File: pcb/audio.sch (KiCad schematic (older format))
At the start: 0 parts

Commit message: pcb: working on sch
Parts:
- added C? (x4): 22uF, symbol Device:C
- added C? (x4): 620pF, symbol Device:C
- added C? (x4): 680pF, symbol Device:C
- added C? (x5): 10uF, symbol Device:C
- added C? (x2): 47uF, symbol Device:CP
- added J?: AudioJack3_Ground_SwitchTR, symbol Connector:AudioJack3_Ground_SwitchTR
- added R? (x4): 750, symbol Device:R
- added R? (x8): 4.99K, symbol Device:R
- added R? (x4): 2.67K, symbol Device:R
- added R? (x4): 2.43K, symbol Device:R
- added R? (x4): 6.81K, symbol Device:R
- added R? (x4): 100, symbol Device:R
- added R? (x4): 100K, symbol Device:R
- added R? (x4): 10K, symbol Device:R
- added R? (x2): 0, symbol Device:R
- added R?: 806, symbol Device:R
- added R?: 1K, symbol Device:R
- added RV?: R_POT_Dual, symbol Device:R_POT_Dual
- added U?: WM8740, footprints:SSOP-28-P0.65, symbol symbols:WM8740
- added U? (x9): ADA4075-2, symbol Amplifier_Operational:ADA4075-2
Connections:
- net labels added: DAC_SYSCLK, GND, SAI1_TXC, SAI1_TXD, SAI1_TXFS, VCOM
- wire segments 0 -> 161

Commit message: pcb: working on sch
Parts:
- removed C? (x4): 22uF, symbol Device:C
- removed C? (x4): 620pF, symbol Device:C
- removed C? (x4): 680pF, symbol Device:C
- removed C? (x5): 10uF, symbol Device:C
- removed C? (x2): 47uF, symbol Device:CP
- removed J?: AudioJack3_Ground_SwitchTR, symbol Connector:AudioJack3_Ground_SwitchTR
- removed R? (x4): 750, symbol Device:R
- removed R? (x8): 4.99K, symbol Device:R
- removed R? (x4): 2.67K, symbol Device:R
- removed R? (x4): 2.43K, symbol Device:R
- removed R? (x4): 6.81K, symbol Device:R
- removed R? (x4): 100, symbol Device:R
- removed R? (x4): 100K, symbol Device:R
- removed R? (x4): 10K, symbol Device:R
- removed R? (x2): 0, symbol Device:R
- removed R?: 806, symbol Device:R
- removed R?: 1K, symbol Device:R
- removed RV?: R_POT_Dual, symbol Device:R_POT_Dual
- removed U?: WM8740, footprints:SSOP-28-P0.65, symbol symbols:WM8740
- removed U? (x9): ADA4075-2, symbol Amplifier_Operational:ADA4075-2
- added C400, C401, C402, C403: 100nF, symbol Device:C
- added C404: 4.7uF, symbol Device:C
- added C405, C408, C409: 1uF, symbol Device:C
- added C406, C407, C412, C413, C414, C415, C416, C417: 2.2uF, symbol Device:C
- added C410, C411: 15uF, symbol Device:C
- added J400: AudioJack4, symbol Connector:AudioJack4
- added L400, L401: 120R, symbol Device:L
- added R400, R401, R402, R403: 33, symbol Device:R
- added R404: 10K, symbol Device:R
- added U400: CS43130, symbol symbols:CS43130
- added U401: ADP150-3.0, Package_TO_SOT_SMD:SOT-23-5, symbol Regulator_Linear:AP2127K-3.0
- added U402, U403: ADP150-1.8, Package_TO_SOT_SMD:SOT-23-5, symbol Regulator_Linear:AP2112K-1.8
- added X400: DSC1001CE2-022.5792, Oscillator:Oscillator_SMD_Abracon_ASE-4Pin_3.2x2.5mm, symbol Oscillator:ASE-xxxMHz
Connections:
- net labels added: +1V8, +3V3, I2C1_SCL, I2C1_SDA, POR, SAI1_MCLK
- net labels removed: DAC_SYSCLK, VCOM
- wire segments 161 -> 90
- no-connect marks 0 -> 4

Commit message: pcb: finishing sch for r0.1
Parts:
- added RV400: RK14J11A0A02, footprints:Potentiometer_RK14J, symbol Device:R_POT
- C400, C401, C402, C403, C405, C406, C407, C408, C409, C412, C413, C414, C415, C416, C417: footprint (none) -> Capacitor_SMD:C_0402_1005Metric
- C404, C410, C411: footprint (none) -> Capacitor_SMD:C_0603_1608Metric
- J400: footprint (none) -> Connector_Audio:Jack_3.5mm_PJ320D_Horizontal
- L400, L401: footprint (none) -> Inductor_SMD:L_0603_1608Metric
- R400, R401, R402, R403, R404: footprint (none) -> Resistor_SMD:R_0603_1608Metric
- U400: footprint (none) -> Package_DFN_QFN:QFN-40-1EP_5x5mm_P0.4mm_EP3.6x3.6mm_ThermalVias
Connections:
- net +3V3: now also RV400.1
- net GND: now also RV400.3
- new net ADC1_IN0: RV400.2

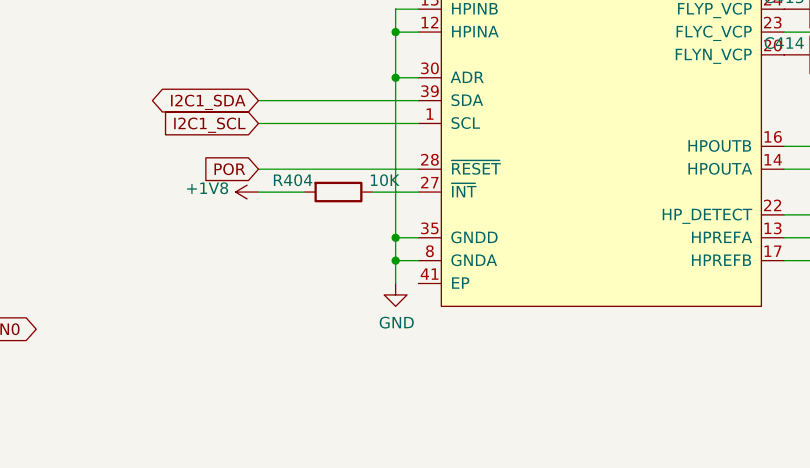
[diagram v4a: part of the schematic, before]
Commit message: pcb: initial netlist
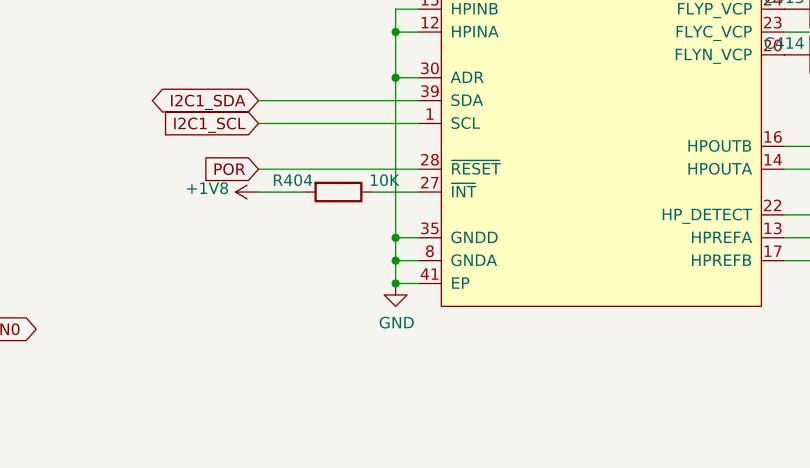
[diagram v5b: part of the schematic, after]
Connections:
- net GND: now also U400.41 (EP)
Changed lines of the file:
@@
 Wire Wire Line
 	2550 5900 2900 5900
+Wire Wire Line
+	5000 5700 4900 5700
+Connection ~ 4900 5700
 $EndSCHEMATC

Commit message: pcb: routing
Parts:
- removed J400: AudioJack4, Connector_Audio:Jack_3.5mm_PJ320D_Horizontal, symbol Connector:AudioJack4
- added J1: AudioJack3_SwitchTR, footprints:Jack_3.5mm_PJ307C, symbol pcb-rescue:AudioJack3_SwitchTR-Connector
- C400, C401, C402, C403, C404, C405, C406, C407, C408, C409, C410, C411, C412, C413, C414, C415, C416, C417: symbol Device:C -> pcb-rescue:C-Device
- L400, L401: symbol Device:L -> pcb-rescue:L-Device
- R400, R401, R402, R403, R404: symbol Device:R -> pcb-rescue:R-Device
- RV400: symbol Device:R_POT -> pcb-rescue:R_POT-Device
- U401: symbol Regulator_Linear:AP2127K-3.0 -> pcb-rescue:AP2127K-3.0-Regulator_Linear
- U402, U403: symbol Regulator_Linear:AP2112K-1.8 -> pcb-rescue:AP2112K-1.8-Regulator_Linear
- X400: symbol Oscillator:ASE-xxxMHz -> pcb-rescue:ASE-xxxMHz-Oscillator
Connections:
- net GND: now also U400.13 (HPREFA), U400.17 (HPREFB), J1.S
- net at U400.16 (HPOUTB): now also J1.R
- net at U400.22 (HP_DETECT): now also J1.TN
- net at U400.14 (HPOUTA): now also J1.T
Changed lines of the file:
@@
 SAI1_TXD
-$Comp
-L Connector:AudioJack4 J400
-U 1 1 5D3B8C10
-P 7850 5100
-F 0 "J400" H 7520 5075 50  0000 R CNN
-F 1 "AudioJack4" H 7520 4984 50  0000 R CNN
-F 2 "Connector_Audio:Jack_3.5mm_PJ320D_Horizontal" H 7850 5100 50  0001 C CNN
-F 3 "~" H 7850 5100 50  0001 C CNN
-	1    7850 5100
-	-1   0    0    -1
-$EndComp
 $Comp
 L symbols:CS43130 U400
@@
 $EndComp
 $Comp
-L Regulator_Linear:AP2112K-1.8 U402
+L pcb-rescue:AP2112K-1.8-Regulator_Linear U402
 U 1 1 5D3BE239
 P 8200 3500
@@
 $EndComp
 $Comp
-L Regulator_Linear:AP2127K-3.0 U401
+L pcb-rescue:AP2127K-3.0-Regulator_Linear U401
 U 1 1 5D3C4251
 P 8200 2500
@@
 $EndComp
 $Comp
-L power:+3V3 #PWR0252
+L pcb-rescue:+3V3-power #PWR0252
 U 1 1 5D3C5E19
 P 8600 2300
@@
 	8500 2500 8600 2500
 $Comp
-L power:GND #PWR0253
+L pcb-rescue:GND-power #PWR0253
 U 1 1 5D3C6CEC
 P 8200 2800
@@
 $EndComp
 $Comp
-L power:GND #PWR0254
+L pcb-rescue:GND-power #PWR0254
 U 1 1 5D3C71EE
 P 8200 3800
@@
 $EndComp
 $Comp
-L Device:C C405
+L pcb-rescue:C-Device C405
 U 1 1 5D3C76A9
 P 8900 2550
@@
 $EndComp
 $Comp
-L Device:C C408
+L pcb-rescue:C-Device C408
 U 1 1 5D3C8004
 P 8900 3550
@@
 $EndComp
 $Comp
-L Device:C C404
+L pcb-rescue:C-Device C404
 U 1 1 5D3C85BE
 P 7600 2550
@@
 $EndComp
 $Comp
-L Device:C C407
+L pcb-rescue:C-Device C407
 U 1 1 5D3C8D9A
 P 7700 3550
@@
 $EndComp
 $Comp
-L Device:C C406
+L pcb-rescue:C-Device C406
 U 1 1 5D3C9210
 P 7300 3650
@@
 $EndComp
 $Comp
-L Device:C C403
+L pcb-rescue:C-Device C403
 U 1 1 5D3C9FD4
 P 7200 2550
@@
 $EndComp
 $Comp
-L power:GND #PWR0255
+L pcb-rescue:GND-power #PWR0255
 U 1 1 5D3CA6E5
 P 7600 2700
@@
 $EndComp
 $Comp
-L power:GND #PWR0256
+L pcb-rescue:GND-power #PWR0256
 U 1 1 5D3CA8EB
 P 7200 2700
@@
 $EndComp
 $Comp
-L power:GND #PWR0257
+L pcb-rescue:GND-power #PWR0257
 U 1 1 5D3CAA8D
 P 8900 2700
@@
 $EndComp
 $Comp
-L power:GND #PWR0258
+L pcb-rescue:GND-power #PWR0258
 U 1 1 5D3CAE2F
 P 8900 3700
@@
 $EndComp
 $Comp
-L power:GND #PWR0259
+L pcb-rescue:GND-power #PWR0259
 U 1 1 5D3CB31E
 P 7700 3700
@@
 $EndComp
 $Comp
-L power:GND #PWR0260
+L pcb-rescue:GND-power #PWR0260
 U 1 1 5D3CB6C2
 P 7300 3800
@@
 Connection ~ 8600 2500
 $Comp
-L Device:C C410
+L pcb-rescue:C-Device C410
 U 1 1 5D3CDB2E
 P 6950 3300
@@
 $EndComp
 $Comp
-L Device:C C411
+L pcb-rescue:C-Device C411
 U 1 1 5D3CEBF2
 P 6950 3600
@@
 $EndComp
 $Comp
-L Device:C C412
+L pcb-rescue:C-Device C412
 U 1 1 5D3D16A3
 P 6950 3800
@@
 	6800 3800 6600 3800
 $Comp
-L Regulator_Linear:AP2112K-1.8 U403
+L pcb-rescue:AP2112K-1.8-Regulator_Linear U403
 U 1 1 5D3DDAF9
 P 8200 4400
@@
 Connection ~ 8600 4300
 $Comp
-L power:GND #PWR0261
+L pcb-rescue:GND-power #PWR0261
 U 1 1 5D3DDB03
 P 8200 4700
@@
 $EndComp
 $Comp
-L Device:C C409
+L pcb-rescue:C-Device C409
 U 1 1 5D3DDB09
 P 8900 4450
@@
 $EndComp
 $Comp
-L Device:C C417
+L pcb-rescue:C-Device C417
 U 1 1 5D3DDB0F
 P 7700 4450
@@
 $EndComp
 $Comp
-L power:GND #PWR0262
+L pcb-rescue:GND-power #PWR0262
 U 1 1 5D3DDB15
 P 8900 4600
@@
 $EndComp
 $Comp
-L power:GND #PWR0263
+L pcb-rescue:GND-power #PWR0263
 U 1 1 5D3DDB1B
 P 7700 4600
@@
 Connection ~ 7700 4300
 $Comp
-L Device:C C416
+L pcb-rescue:C-Device C416
 U 1 1 5D3E2D8A
 P 7400 4350
@@
 $EndComp
 $Comp
-L Device:C C415
+L pcb-rescue:C-Device C415
 U 1 1 5D3E3537
 P 7100 4450
@@
 $EndComp
 $Comp
-L Device:C C413
+L pcb-rescue:C-Device C413
 U 1 1 5D3E42FA
 P 6750 4500
@@
 $EndComp
 $Comp
-L Device:C C414
+L pcb-rescue:C-Device C414
 U 1 1 5D3E4B00
 P 6750 4700
@@
 $EndComp
 $Comp
-L power:GND #PWR0264
+L pcb-rescue:GND-power #PWR0264
 U 1 1 5D3E50F6
 P 7400 4500
@@
 $EndComp
 $Comp
-L power:GND #PWR0265
+L pcb-rescue:GND-power #PWR0265
 U 1 1 5D3E5385
 P 7100 4600
@@
 $EndComp
 $Comp
-L power:GND #PWR0266
+L pcb-rescue:GND-power #PWR0266
 U 1 1 5D3E55AD
 P 6600 4400
@@
 	7550 5000 7650 5000
 Wire Wire Line
-	6600 5400 7350 5400
-Wire Wire Line
-	7350 5400 7350 5100
-Wire Wire Line
-	7350 5100 7650 5100
-Wire Wire Line
-	6600 5100 7250 5100
-Wire Wire Line
-	7250 5100 7250 5200
-Wire Wire Line
-	7250 5200 7650 5200
-Wire Wire Line
 	7650 5300 7150 5300
 Wire Wire Line
@@
 	7150 5200 6600 5200
 $Comp
-L power:+1V8 #PWR0267
+L pcb-rescue:+1V8-power #PWR0267
 U 1 1 5D40EC46
 P 4200 2300
@@
 $EndComp
 $Comp
-L Device:C C402
+L pcb-rescue:C-Device C402
 U 1 1 5D412186
 P 4600 2750
@@
 $EndComp
 $Comp
-L power:GND #PWR0268
+L pcb-rescue:GND-power #PWR0268
 U 1 1 5D41218C
 P 4600 2900
@@
 $EndComp
 $Comp
-L Device:C C401
+L pcb-rescue:C-Device C401
 U 1 1 5D414243
 P 4200 2750
@@
 $EndComp
 $Comp
-L power:GND #PWR0269
+L pcb-rescue:GND-power #PWR0269
 U 1 1 5D414249
 P 4200 2900
@@
 SAI1_MCLK
 $Comp
-L Device:R R400
+L pcb-rescue:R-Device R400
 U 1 1 5D42CABC
 P 4650 3300
@@
 $EndComp
 $Comp
-L Device:R R401
+L pcb-rescue:R-Device R401
 U 1 1 5D437A63
 P 4650 4100
@@
 $EndComp
 $Comp
-L Device:R R402
+L pcb-rescue:R-Device R402
 U 1 1 5D438FF1
 P 4650 4200
@@
 $EndComp
 $Comp
-L Device:R R403
+L pcb-rescue:R-Device R403
 U 1 1 5D4391CB
 P 4650 4300
@@
 	4800 4300 5000 4300
 $Comp
-L power:GND #PWR0270
+L pcb-rescue:GND-power #PWR0270
 U 1 1 5D44FB8A
 P 4900 5700
@@
 	4300 5200 5000 5200
 $Comp
-L Device:R R404
+L pcb-rescue:R-Device R404
 U 1 1 5D46D440
 P 4650 5300
@@
 $EndComp
 $Comp
-L power:+1V8 #PWR0271
+L pcb-rescue:+1V8-power #PWR0271
 U 1 1 5D46FEBD
 P 4300 5300
@@
 NoConn ~ 5000 3600
 $Comp
-L Oscillator:ASE-xxxMHz X400
+L pcb-rescue:ASE-xxxMHz-Oscillator X400
 U 1 1 5D484130
 P 3500 3500
@@
 $EndComp
 $Comp
-L power:+1V8 #PWR0272
+L pcb-rescue:+1V8-power #PWR0272
 U 1 1 5D485FE4
 P 3500 2300
@@
 $EndComp
 $Comp
-L Device:C C400
+L pcb-rescue:C-Device C400
 U 1 1 5D487832
 P 3100 2750
@@
 $EndComp
 $Comp
-L power:GND #PWR0273
+L pcb-rescue:GND-power #PWR0273
 U 1 1 5D487838
 P 3100 2900
@@
 Connection ~ 3500 2600
 $Comp
-L power:GND #PWR0274
+L pcb-rescue:GND-power #PWR0274
 U 1 1 5D490333
 P 3500 3800
@@
 	3800 3500 5000 3500
 $Comp
-L Device:L L401
+L pcb-rescue:L-Device L401
 U 1 1 5D4971D8
 P 4200 2450
@@
 $EndComp
 $Comp
-L Device:L L400
+L pcb-rescue:L-Device L400
 U 1 1 5D4999E2
 P 3500 2450
@@
 $EndComp
 $Comp
-L Device:R_POT RV?
+L pcb-rescue:R_POT-Device RV?
 U 1 1 5D1F1382
 P 2400 5900
@@
 $EndComp
 $Comp
-L power:GND #PWR0275
+L pcb-rescue:GND-power #PWR0275
 U 1 1 5D1F4706
 P 2400 6200
@@
 $EndComp
 $Comp
-L power:+3V3 #PWR0276
+L pcb-rescue:+3V3-power #PWR0276
 U 1 1 5D1F4C5C
 P 2400 5600
@@
 	5000 5700 4900 5700
 Connection ~ 4900 5700
+$Comp
+L pcb-rescue:AudioJack3_SwitchTR-Connector J1
+U 1 1 5D440F5D
+P 7850 5100
+F 0 "J1" H 7570 5025 50  0000 R CNN
+F 1 "AudioJack3_SwitchTR" H 7570 4934 50  0000 R CNN
+F 2 "footprints:Jack_3.5mm_PJ307C" H 7850 5100 50  0001 C CNN
+F 3 "~" H 7850 5100 50  0001 C CNN
+	1    7850 5100
+	-1   0    0    -1
+$EndComp
+Wire Wire Line
+	6600 5100 7650 5100
+$Comp
+L pcb-rescue:GND-power #PWR0165
+U 1 1 5D462232
+P 7550 5000
+F 0 "#PWR0165" H 7550 4750 50  0001 C CNN
+F 1 "GND" H 7555 4827 50  0000 C CNN
+F 2 "" H 7550 5000 50  0001 C CNN
+F 3 "" H 7550 5000 50  0001 C CNN
+	1    7550 5000
+	-1   0    0    1
+$EndComp
+Wire Wire Line
+	6600 5400 7650 5400
 $EndSCHEMATC

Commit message: pcb: rev 0.1
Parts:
- C400, C401, C402, C403, C404, C405, C406, C407, C408, C409, C410, C411, C412, C413, C414, C415, C416, C417: symbol pcb-rescue:C-Device -> pcb-rescue:C-Device-pcb-rescue
- J1: symbol pcb-rescue:AudioJack3_SwitchTR-Connector -> pcb-rescue:AudioJack3_SwitchTR-Connector-pcb-rescue
- L400, L401: symbol pcb-rescue:L-Device -> pcb-rescue:L-Device-pcb-rescue
- R400, R401, R402, R403, R404: symbol pcb-rescue:R-Device -> pcb-rescue:R-Device-pcb-rescue
- RV400: symbol pcb-rescue:R_POT-Device -> pcb-rescue:R_POT-Device-pcb-rescue
- U401: symbol pcb-rescue:AP2127K-3.0-Regulator_Linear -> pcb-rescue:AP2127K-3.0-Regulator_Linear-pcb-rescue
- U402, U403: symbol pcb-rescue:AP2112K-1.8-Regulator_Linear -> pcb-rescue:AP2112K-1.8-Regulator_Linear-pcb-rescue
- X400: symbol pcb-rescue:ASE-xxxMHz-Oscillator -> pcb-rescue:ASE-xxxMHz-Oscillator-pcb-rescue
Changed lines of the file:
@@
 encoding utf-8
 Sheet 7 11
-Title "Audio Output"
-Date ""
+Title "RhythmPocket"
+Date "2019-07-16"
 Rev "R0.1"
 Comp "ZephRay"
@@
 $EndComp
 $Comp
-L pcb-rescue:AP2112K-1.8-Regulator_Linear U402
+L pcb-rescue:AP2112K-1.8-Regulator_Linear-pcb-rescue U402
 U 1 1 5D3BE239
 P 8200 3500
@@
 $EndComp
 $Comp
-L pcb-rescue:AP2127K-3.0-Regulator_Linear U401
+L pcb-rescue:AP2127K-3.0-Regulator_Linear-pcb-rescue U401
 U 1 1 5D3C4251
 P 8200 2500
@@
 $EndComp
 $Comp
-L pcb-rescue:+3V3-power #PWR0252
+L pcb-rescue:+3V3-power-pcb-rescue #PWR0252
 U 1 1 5D3C5E19
 P 8600 2300
@@
 	8500 2500 8600 2500
 $Comp
-L pcb-rescue:GND-power #PWR0253
+L pcb-rescue:GND-power-pcb-rescue #PWR0253
 U 1 1 5D3C6CEC
 P 8200 2800
@@
 $EndComp
 $Comp
-L pcb-rescue:GND-power #PWR0254
+L pcb-rescue:GND-power-pcb-rescue #PWR0254
 U 1 1 5D3C71EE
 P 8200 3800
@@
 $EndComp
 $Comp
-L pcb-rescue:C-Device C405
+L pcb-rescue:C-Device-pcb-rescue C405
 U 1 1 5D3C76A9
 P 8900 2550
@@
 $EndComp
 $Comp
-L pcb-rescue:C-Device C408
+L pcb-rescue:C-Device-pcb-rescue C408
 U 1 1 5D3C8004
 P 8900 3550
@@
 $EndComp
 $Comp
-L pcb-rescue:C-Device C404
+L pcb-rescue:C-Device-pcb-rescue C404
 U 1 1 5D3C85BE
 P 7600 2550
@@
 $EndComp
 $Comp
-L pcb-rescue:C-Device C407
+L pcb-rescue:C-Device-pcb-rescue C407
 U 1 1 5D3C8D9A
 P 7700 3550
@@
 $EndComp
 $Comp
-L pcb-rescue:C-Device C406
+L pcb-rescue:C-Device-pcb-rescue C406
 U 1 1 5D3C9210
 P 7300 3650
@@
 $EndComp
 $Comp
-L pcb-rescue:C-Device C403
+L pcb-rescue:C-Device-pcb-rescue C403
 U 1 1 5D3C9FD4
 P 7200 2550
@@
 $EndComp
 $Comp
-L pcb-rescue:GND-power #PWR0255
+L pcb-rescue:GND-power-pcb-rescue #PWR0255
 U 1 1 5D3CA6E5
 P 7600 2700
@@
 $EndComp
 $Comp
-L pcb-rescue:GND-power #PWR0256
+L pcb-rescue:GND-power-pcb-rescue #PWR0256
 U 1 1 5D3CA8EB
 P 7200 2700
@@
 $EndComp
 $Comp
-L pcb-rescue:GND-power #PWR0257
+L pcb-rescue:GND-power-pcb-rescue #PWR0257
 U 1 1 5D3CAA8D
 P 8900 2700
@@
 $EndComp
 $Comp
-L pcb-rescue:GND-power #PWR0258
+L pcb-rescue:GND-power-pcb-rescue #PWR0258
 U 1 1 5D3CAE2F
 P 8900 3700
@@
 $EndComp
 $Comp
-L pcb-rescue:GND-power #PWR0259
+L pcb-rescue:GND-power-pcb-rescue #PWR0259
 U 1 1 5D3CB31E
 P 7700 3700
@@
 $EndComp
 $Comp
-L pcb-rescue:GND-power #PWR0260
+L pcb-rescue:GND-power-pcb-rescue #PWR0260
 U 1 1 5D3CB6C2
 P 7300 3800
@@
 Connection ~ 8600 2500
 $Comp
-L pcb-rescue:C-Device C410
+L pcb-rescue:C-Device-pcb-rescue C410
 U 1 1 5D3CDB2E
 P 6950 3300
@@
 $EndComp
 $Comp
-L pcb-rescue:C-Device C411
+L pcb-rescue:C-Device-pcb-rescue C411
 U 1 1 5D3CEBF2
 P 6950 3600
@@
 $EndComp
 $Comp
-L pcb-rescue:C-Device C412
+L pcb-rescue:C-Device-pcb-rescue C412
 U 1 1 5D3D16A3
 P 6950 3800
@@
 	6800 3800 6600 3800
 $Comp
-L pcb-rescue:AP2112K-1.8-Regulator_Linear U403
+L pcb-rescue:AP2112K-1.8-Regulator_Linear-pcb-rescue U403
 U 1 1 5D3DDAF9
 P 8200 4400
@@
 Connection ~ 8600 4300
 $Comp
-L pcb-rescue:GND-power #PWR0261
+L pcb-rescue:GND-power-pcb-rescue #PWR0261
 U 1 1 5D3DDB03
 P 8200 4700
@@
 $EndComp
 $Comp
-L pcb-rescue:C-Device C409
+L pcb-rescue:C-Device-pcb-rescue C409
 U 1 1 5D3DDB09
 P 8900 4450
@@
 $EndComp
 $Comp
-L pcb-rescue:C-Device C417
+L pcb-rescue:C-Device-pcb-rescue C417
 U 1 1 5D3DDB0F
 P 7700 4450
@@
 $EndComp
 $Comp
-L pcb-rescue:GND-power #PWR0262
+L pcb-rescue:GND-power-pcb-rescue #PWR0262
 U 1 1 5D3DDB15
 P 8900 4600
@@
 $EndComp
 $Comp
-L pcb-rescue:GND-power #PWR0263
+L pcb-rescue:GND-power-pcb-rescue #PWR0263
 U 1 1 5D3DDB1B
 P 7700 4600
@@
 Connection ~ 7700 4300
 $Comp
-L pcb-rescue:C-Device C416
+L pcb-rescue:C-Device-pcb-rescue C416
 U 1 1 5D3E2D8A
 P 7400 4350
@@
 $EndComp
 $Comp
-L pcb-rescue:C-Device C415
+L pcb-rescue:C-Device-pcb-rescue C415
 U 1 1 5D3E3537
 P 7100 4450
@@
 $EndComp
 $Comp
-L pcb-rescue:C-Device C413
+L pcb-rescue:C-Device-pcb-rescue C413
 U 1 1 5D3E42FA
 P 6750 4500
@@
 $EndComp
 $Comp
-L pcb-rescue:C-Device C414
+L pcb-rescue:C-Device-pcb-rescue C414
 U 1 1 5D3E4B00
 P 6750 4700
@@
 $EndComp
 $Comp
-L pcb-rescue:GND-power #PWR0264
+L pcb-rescue:GND-power-pcb-rescue #PWR0264
 U 1 1 5D3E50F6
 P 7400 4500
@@
 $EndComp
 $Comp
-L pcb-rescue:GND-power #PWR0265
+L pcb-rescue:GND-power-pcb-rescue #PWR0265
 U 1 1 5D3E5385
 P 7100 4600
@@
 $EndComp
 $Comp
-L pcb-rescue:GND-power #PWR0266
+L pcb-rescue:GND-power-pcb-rescue #PWR0266
 U 1 1 5D3E55AD
 P 6600 4400
@@
 	7150 5200 6600 5200
 $Comp
-L pcb-rescue:+1V8-power #PWR0267
+L pcb-rescue:+1V8-power-pcb-rescue #PWR0267
 U 1 1 5D40EC46
 P 4200 2300
@@
 $EndComp
 $Comp
-L pcb-rescue:C-Device C402
+L pcb-rescue:C-Device-pcb-rescue C402
 U 1 1 5D412186
 P 4600 2750
@@
 $EndComp
 $Comp
-L pcb-rescue:GND-power #PWR0268
+L pcb-rescue:GND-power-pcb-rescue #PWR0268
 U 1 1 5D41218C
 P 4600 2900
@@
 $EndComp
 $Comp
-L pcb-rescue:C-Device C401
+L pcb-rescue:C-Device-pcb-rescue C401
 U 1 1 5D414243
 P 4200 2750
@@
 $EndComp
 $Comp
-L pcb-rescue:GND-power #PWR0269
+L pcb-rescue:GND-power-pcb-rescue #PWR0269
 U 1 1 5D414249
 P 4200 2900
@@
 SAI1_MCLK
 $Comp
-L pcb-rescue:R-Device R400
+L pcb-rescue:R-Device-pcb-rescue R400
 U 1 1 5D42CABC
 P 4650 3300
@@
 $EndComp
 $Comp
-L pcb-rescue:R-Device R401
+L pcb-rescue:R-Device-pcb-rescue R401
 U 1 1 5D437A63
 P 4650 4100
@@
 $EndComp
 $Comp
-L pcb-rescue:R-Device R402
+L pcb-rescue:R-Device-pcb-rescue R402
 U 1 1 5D438FF1
 P 4650 4200
@@
 $EndComp
 $Comp
-L pcb-rescue:R-Device R403
+L pcb-rescue:R-Device-pcb-rescue R403
 U 1 1 5D4391CB
 P 4650 4300
@@
 	4800 4300 5000 4300
 $Comp
-L pcb-rescue:GND-power #PWR0270
+L pcb-rescue:GND-power-pcb-rescue #PWR0270
 U 1 1 5D44FB8A
 P 4900 5700
@@
 	4300 5200 5000 5200
 $Comp
-L pcb-rescue:R-Device R404
+L pcb-rescue:R-Device-pcb-rescue R404
 U 1 1 5D46D440
 P 4650 5300
@@
 $EndComp
 $Comp
-L pcb-rescue:+1V8-power #PWR0271
+L pcb-rescue:+1V8-power-pcb-rescue #PWR0271
 U 1 1 5D46FEBD
 P 4300 5300
@@
 NoConn ~ 5000 3600
 $Comp
-L pcb-rescue:ASE-xxxMHz-Oscillator X400
+L pcb-rescue:ASE-xxxMHz-Oscillator-pcb-rescue X400
 U 1 1 5D484130
 P 3500 3500
@@
 $EndComp
 $Comp
-L pcb-rescue:+1V8-power #PWR0272
+L pcb-rescue:+1V8-power-pcb-rescue #PWR0272
 U 1 1 5D485FE4
 P 3500 2300
@@
 $EndComp
 $Comp
-L pcb-rescue:C-Device C400
+L pcb-rescue:C-Device-pcb-rescue C400
 U 1 1 5D487832
 P 3100 2750
@@
 $EndComp
 $Comp
-L pcb-rescue:GND-power #PWR0273
+L pcb-rescue:GND-power-pcb-rescue #PWR0273
 U 1 1 5D487838
 P 3100 2900
@@
 Connection ~ 3500 2600
 $Comp
-L pcb-rescue:GND-power #PWR0274
+L pcb-rescue:GND-power-pcb-rescue #PWR0274
 U 1 1 5D490333
 P 3500 3800
@@
 	3800 3500 5000 3500
 $Comp
-L pcb-rescue:L-Device L401
+L pcb-rescue:L-Device-pcb-rescue L401
 U 1 1 5D4971D8
 P 4200 2450
@@
 $EndComp
 $Comp
-L pcb-rescue:L-Device L400
+L pcb-rescue:L-Device-pcb-rescue L400
 U 1 1 5D4999E2
 P 3500 2450
@@
 $EndComp
 $Comp
-L pcb-rescue:R_POT-Device RV?
+L pcb-rescue:R_POT-Device-pcb-rescue RV?
 U 1 1 5D1F1382
 P 2400 5900
@@
 $EndComp
 $Comp
-L pcb-rescue:GND-power #PWR0275
+L pcb-rescue:GND-power-pcb-rescue #PWR0275
 U 1 1 5D1F4706
 P 2400 6200
@@
 $EndComp
 $Comp
-L pcb-rescue:+3V3-power #PWR0276
+L pcb-rescue:+3V3-power-pcb-rescue #PWR0276
 U 1 1 5D1F4C5C
 P 2400 5600
@@
 Connection ~ 4900 5700
 $Comp
-L pcb-rescue:AudioJack3_SwitchTR-Connector J1
+L pcb-rescue:AudioJack3_SwitchTR-Connector-pcb-rescue J1
 U 1 1 5D440F5D
 P 7850 5100
@@
 	6600 5100 7650 5100
 $Comp
-L pcb-rescue:GND-power #PWR0165
+L pcb-rescue:GND-power-pcb-rescue #PWR0165
 U 1 1 5D462232
 P 7550 5000
